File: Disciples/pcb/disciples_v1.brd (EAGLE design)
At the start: 19 x 108.4 mm, 106 parts, among them IC1 OPA1641, IC2 LM324PW, IC3 LM324PW, IC4 TL072D, IC5 LM324PW, IC6 LM4040B10, IC7 LM4040B50, J1 PJ301_THONKICONN6, J10 PJ301_THONKICONN6, J11 PJ301_THONKICONN6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

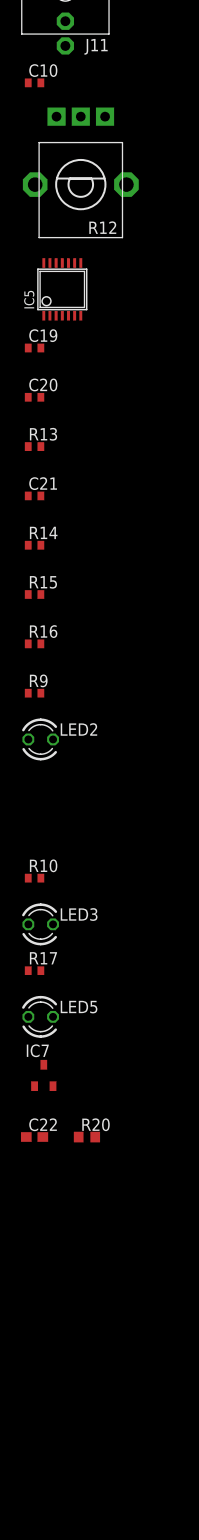
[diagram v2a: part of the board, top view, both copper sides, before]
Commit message: Comparator
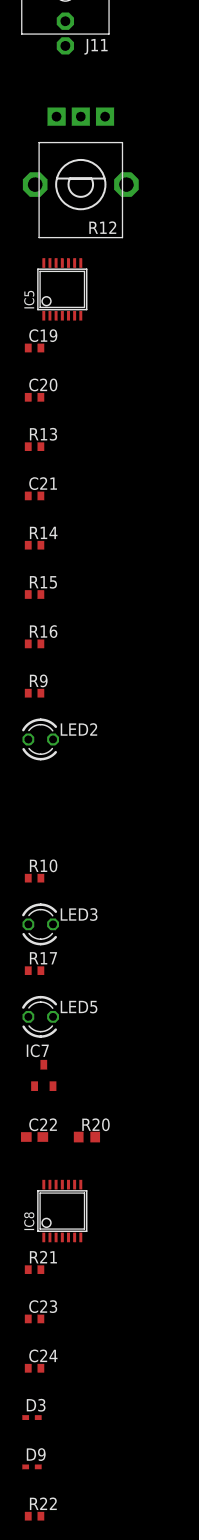
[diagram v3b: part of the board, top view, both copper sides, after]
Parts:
- removed C10: 68p, rcl:C0402
- added C23, C24: 100n, rcl:C0402
- added D3, D9: 1N4148, diode:SOD523
- added IC8: LM324PW, og-ics:TSSOP14
- added R21, R22: 1k, rcl:R0402
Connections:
- new net COMP_-12_+12: IC8.1, R21.1
- new net N$47: IC8.3, R15.2
- new net N$49: J6.P3, R22.1
- new net N$51: D3.C, IC8.7
- new net N$52: D9.A, IC8.8
- net AREF_+5: now also IC8.5
- net COMP: now also D3.A, D9.C, IC8.12, IC8.6, IC8.9, R21.2
- net GND: now also C23.2, C24.1, IC8.10
- net N$27: now also R22.2; no longer J6.P3
- net N$37: now also IC8.13
- net N$38: now also IC8.14
- net N$45: now also IC8.2
- net VCC: now also C23.1, IC8.4
- net VEE: now also C24.2, IC8.11
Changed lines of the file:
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@@
 <attribute name="NAME" x="8.31" y="-374.8875" size="1.27" layer="25" rot="R180"/>
-</element>
-<element name="C10" library="rcl" package="C0402" value="68p" x="0.635" y="-379.4125" smashed="yes">
-<attribute name="NAME" x="0" y="-378.7775" size="1.27" layer="25"/>
-<attribute name="VALUE" x="0" y="-381.3175" size="1.27" layer="27"/>
 </element>
 <element name="R12" library="og-pots" package="ALPS_POT_VERTICAL_PS" value="50k" x="5.3975" y="-389.89" smashed="yes">
@@
 <attribute name="NAME" x="0" y="-487.3625" size="1.27" layer="25"/>
 <attribute name="VALUE" x="0" y="-489.9025" size="1.27" layer="27"/>
+</element>
+<element name="IC8" library="og-ics" package="TSSOP14" value="LM324PW" x="3.4925" y="-495.6175" smashed="yes">
+<attribute name="NAME" x="0.5969" y="-497.7003" size="1.016" layer="25" ratio="10" rot="R90"/>
+<attribute name="VALUE" x="7.3787" y="-497.7003" size="1.016" layer="27" ratio="10" rot="R90"/>
+</element>
+<element name="R21" library="rcl" package="R0402" value="1k" x="0.635" y="-501.65" smashed="yes">
+<attribute name="NAME" x="0" y="-501.015" size="1.27" layer="25"/>
+<attribute name="VALUE" x="0" y="-503.555" size="1.27" layer="27"/>
+</element>
+<element name="C23" library="rcl" package="C0402" value="100n" x="0.635" y="-506.73" smashed="yes">
+<attribute name="NAME" x="0" y="-506.095" size="1.27" layer="25"/>
+<attribute name="VALUE" x="0" y="-508.635" size="1.27" layer="27"/>
+</element>
+<element name="C24" library="rcl" package="C0402" value="100n" x="0.635" y="-511.81" smashed="yes">
+<attribute name="NAME" x="0" y="-511.175" size="1.27" layer="25"/>
+<attribute name="VALUE" x="0" y="-513.715" size="1.27" layer="27"/>
+</element>
+<element name="D3" library="diode" package="SOD523" value="1N4148" x="0.3175" y="-516.89" smashed="yes">
+<attribute name="NAME" x="-0.3175" y="-516.255" size="1.27" layer="25"/>
+<attribute name="VALUE" x="-0.3175" y="-518.795" size="1.27" layer="27"/>
+</element>
+<element name="D9" library="diode" package="SOD523" value="1N4148" x="0.3175" y="-521.97" smashed="yes">
+<attribute name="NAME" x="-0.3175" y="-521.335" size="1.27" layer="25"/>
+<attribute name="VALUE" x="-0.3175" y="-523.875" size="1.27" layer="27"/>
+</element>
+<element name="R22" library="rcl" package="R0402" value="1k" x="0.635" y="-527.05" smashed="yes">
+<attribute name="NAME" x="0" y="-526.415" size="1.27" layer="25"/>
+<attribute name="VALUE" x="0" y="-528.955" size="1.27" layer="27"/>
 </element>
 </elements>
@@
 <contactref element="IC7" pad="2"/>
 <contactref element="C22" pad="2"/>
+<contactref element="C24" pad="1"/>
+<contactref element="C23" pad="2"/>
+<contactref element="IC8" pad="10"/>
+<wire x1="-0.015" y1="-511.81" x2="1.285" y2="-506.73" width="0" layer="19" extent="1-1"/>
+<wire x1="4.1275" y1="-492.8997" x2="1.285" y2="-506.73" width="0" layer="19" extent="1-1"/>
+<wire x1="1.485" y1="-487.9975" x2="4.1275" y2="-492.8997" width="0" layer="19" extent="1-1"/>
 <wire x1="2.5375" y1="-482.7475" x2="1.485" y2="-487.9975" width="0" layer="19" extent="1-1"/>
 <wire x1="1.285" y1="-470.8525" x2="2.5375" y2="-482.7475" width="0" layer="19" extent="1-1"/>
@@
 <contactref element="IC5" pad="11"/>
 <contactref element="C20" pad="2"/>
+<contactref element="IC8" pad="11"/>
+<contactref element="C24" pad="2"/>
+<wire x1="1.285" y1="-511.81" x2="3.4925" y2="-492.8997" width="0" layer="19" extent="1-1"/>
+<wire x1="1.285" y1="-411.7975" x2="3.4925" y2="-492.8997" width="0" layer="19" extent="1-1"/>
 <wire x1="3.4925" y1="-397.9672" x2="1.285" y2="-411.7975" width="0" layer="19" extent="1-1"/>
 <wire x1="1.285" y1="-302.5775" x2="3.4925" y2="-397.9672" width="0" layer="19" extent="1-1"/>
@@
 <contactref element="C19" pad="1"/>
 <contactref element="R20" pad="1"/>
+<contactref element="IC8" pad="4"/>
+<contactref element="C23" pad="1"/>
+<wire x1="3.4925" y1="-498.3353" x2="-0.015" y2="-506.73" width="0" layer="19" extent="1-1"/>
+<wire x1="5.1825" y1="-487.9975" x2="3.4925" y2="-498.3353" width="0" layer="19" extent="1-1"/>
 <wire x1="-0.015" y1="-406.7175" x2="5.1825" y2="-487.9975" width="0" layer="19" extent="1-1"/>
 <wire x1="3.4925" y1="-403.4028" x2="-0.015" y2="-406.7175" width="0" layer="19" extent="1-1"/>
@@
 <signal name="COMP">
 <contactref element="R33" pad="1"/>
+<contactref element="IC8" pad="12"/>
+<contactref element="IC8" pad="6"/>
+<contactref element="R21" pad="2"/>
+<contactref element="D3" pad="A"/>
+<contactref element="D9" pad="C"/>
+<contactref element="IC8" pad="9"/>
+<wire x1="4.7625" y1="-498.3353" x2="1.285" y2="-501.65" width="0" layer="19" extent="1-1"/>
+<wire x1="4.7625" y1="-492.8997" x2="4.7625" y2="-498.3353" width="0" layer="19" extent="1-1"/>
+<wire x1="2.8575" y1="-492.8997" x2="4.7625" y2="-492.8997" width="0" layer="19" extent="1-1"/>
+<wire x1="1.0175" y1="-516.89" x2="1.285" y2="-501.65" width="0" layer="19" extent="1-1"/>
+<wire x1="-0.2825" y1="-521.97" x2="1.0175" y2="-516.89" width="0" layer="19" extent="1-1"/>
+<wire x1="9.8275" y1="-108.2675" x2="4.7625" y2="-492.8997" width="0" layer="19" extent="1-1"/>
 </signal>
 <signal name="N$28">
@@
 <wire x1="2.2225" y1="-403.4028" x2="1.285" y2="-461.3275" width="0" layer="19" extent="1-1"/>
 </signal>
-<signal name="N$27">
-<contactref element="C17" pad="1"/>
-<contactref element="J6" pad="P3"/>
-<wire x1="-0.215" y1="-292.4175" x2="3.81" y2="-50.165" width="0" layer="19" extent="1-1"/>
-</signal>
 <signal name="N$32">
 <contactref element="C17" pad="2"/>
@@
 <signal name="N$45">
 <contactref element="R16" pad="2"/>
+<contactref element="IC8" pad="2"/>
+<wire x1="1.285" y1="-437.1975" x2="2.2225" y2="-498.3353" width="0" layer="19" extent="1-1"/>
 </signal>
 <signal name="N$46">
@@
 <contactref element="R17" pad="1"/>
 <contactref element="LED5" pad="K"/>
+<contactref element="IC8" pad="13"/>
+<wire x1="2.54" y1="-475.615" x2="2.2225" y2="-492.8997" width="0" layer="19" extent="1-1"/>
 <wire x1="-0.015" y1="-470.8525" x2="2.54" y2="-475.615" width="0" layer="19" extent="1-1"/>
 </signal>
 <signal name="N$38">
 <contactref element="LED5" pad="A"/>
+<contactref element="IC8" pad="14"/>
+<wire x1="0" y1="-475.615" x2="1.5875" y2="-492.8997" width="0" layer="19" extent="1-1"/>
 </signal>
 <signal name="AREF_+5">
@@
 <contactref element="R20" pad="2"/>
 <contactref element="C22" pad="1"/>
+<contactref element="IC8" pad="5"/>
+<wire x1="6.8825" y1="-487.9975" x2="4.1275" y2="-498.3353" width="0" layer="19" extent="1-1"/>
+<wire x1="-0.215" y1="-487.9975" x2="6.8825" y2="-487.9975" width="0" layer="19" extent="1-1"/>
 <wire x1="0.6375" y1="-482.7475" x2="-0.215" y2="-487.9975" width="0" layer="19" extent="1-1"/>
-<wire x1="6.8825" y1="-487.9975" x2="-0.215" y2="-487.9975" width="0" layer="19" extent="1-1"/>
+</signal>
+<signal name="N$47">
+<contactref element="R15" pad="2"/>
+<contactref element="IC8" pad="3"/>
+<wire x1="1.285" y1="-432.1175" x2="2.8575" y2="-498.3353" width="0" layer="19" extent="1-1"/>
+</signal>
+<signal name="COMP_-12_+12">
+<contactref element="IC8" pad="1"/>
+<contactref element="R21" pad="1"/>
+<wire x1="1.5875" y1="-498.3353" x2="-0.015" y2="-501.65" width="0" layer="19" extent="1-1"/>
+</signal>
+<signal name="N$51">
+<contactref element="IC8" pad="7"/>
+<contactref element="D3" pad="C"/>
+<wire x1="-0.2825" y1="-516.89" x2="5.3975" y2="-498.3353" width="0" layer="19" extent="1-1"/>
+</signal>
+<signal name="N$52">
+<contactref element="IC8" pad="8"/>
+<contactref element="D9" pad="A"/>
+<wire x1="1.0175" y1="-521.97" x2="5.3975" y2="-492.8997" width="0" layer="19" extent="1-1"/>
+</signal>
+<signal name="N$27">
+<contactref element="R22" pad="2"/>
+<contactref element="C17" pad="1"/>
+<wire x1="1.285" y1="-527.05" x2="-0.215" y2="-292.4175" width="0" layer="19" extent="1-1"/>
+</signal>
+<signal name="N$49">
+<contactref element="J6" pad="P3"/>
+<contactref element="R22" pad="1"/>
+<wire x1="-0.015" y1="-527.05" x2="3.81" y2="-50.165" width="0" layer="19" extent="1-1"/>
 </signal>
 </signals>

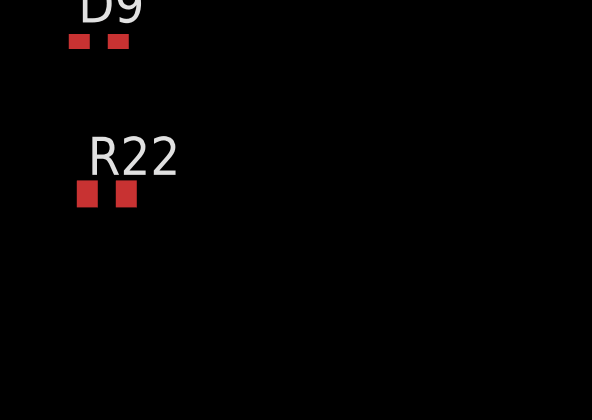
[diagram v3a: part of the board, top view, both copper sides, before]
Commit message: Added slow slew cap (no sw yet)
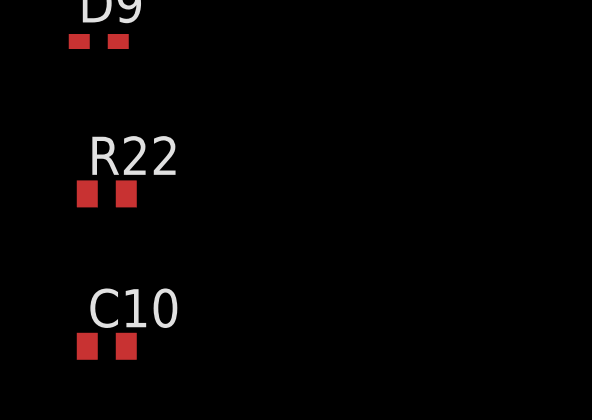
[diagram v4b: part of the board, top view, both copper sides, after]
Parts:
- added C10: 100u, rcl:C0402
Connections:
- net SLEW: now also C10.2
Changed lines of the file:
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@@
 <attribute name="VALUE" x="0" y="-528.955" size="1.27" layer="27"/>
+</element>
+<element name="C10" library="rcl" package="C0402" value="100u" x="0.635" y="-532.13" smashed="yes">
+<attribute name="NAME" x="0" y="-531.495" size="1.27" layer="25"/>
+<attribute name="VALUE" x="0" y="-534.035" size="1.27" layer="27"/>
 </element>
 </elements>
@@
 </signal>
 <signal name="SLEW">
-<contactref element="C11" pad="2"/>
 <contactref element="R28" pad="2"/>
 <contactref element="R2" pad="1"/>
@@
 <contactref element="J8" pad="P2"/>
 <contactref element="IC5" pad="3"/>
-<wire x1="1.6025" y1="-223.2025" x2="6.365" y2="-228.2825" width="0" layer="19" extent="1-1"/>
+<contactref element="C11" pad="2"/>
+<contactref element="C10" pad="2"/>
+<wire x1="6.365" y1="-228.2825" x2="1.6025" y2="-223.2025" width="0" layer="19" extent="1-1"/>
 <wire x1="3.81" y1="-341.9475" x2="6.365" y2="-228.2825" width="0" layer="19" extent="1-1"/>
 <wire x1="2.8575" y1="-403.4028" x2="3.81" y2="-341.9475" width="0" layer="19" extent="1-1"/>
+<wire x1="1.285" y1="-532.13" x2="2.8575" y2="-403.4028" width="0" layer="19" extent="1-1"/>
 <wire x1="0.3025" y1="-90.17" x2="1.6025" y2="-223.2025" width="0" layer="19" extent="1-1"/>
 <wire x1="12.2428" y1="10.16" x2="0.3025" y2="-90.17" width="0" layer="19" extent="1-1"/>
@@
 <contactref element="R18" pad="P$2"/>
 <contactref element="R19" pad="P$2"/>
+<contactref element="IC3" pad="9"/>
 <contactref element="C11" pad="1"/>
-<contactref element="IC3" pad="9"/>
 <wire x1="5.3975" y1="-306.055" x2="5.065" y2="-228.2825" width="0" layer="19" extent="1-1"/>
 <wire x1="5.3975" y1="-320.025" x2="5.3975" y2="-306.055" width="0" layer="19" extent="1-1"/>

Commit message: CV Pot
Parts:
- added C25, C26: 100n, rcl:C0402
- added IC9: LM324PW, og-ics:TSSOP14
- added J12: PJ301_THONKICONN6, og-pj301:WQP_PJ_301M6
- added R24: 50k, og-pots:ALPS_POT_VERTICAL_PS
- added R27: 510, rcl:R0402
- C21: value TBD -> (none)
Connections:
- new net N$50: IC9.3, R24.P$2
- new net N$53: J12.P3, R27.2
- net AREF_+5: now also R24.P$3
- net GND: now also C25.2, C26.1, J12.P1
- net THRESH: now also IC9.1, IC9.2, R27.1
- net VCC: now also C25.1, IC9.4
- net VEE: now also C26.2, IC9.11
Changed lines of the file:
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@@
 <attribute name="VALUE" x="0" y="-418.7825" size="1.27" layer="27"/>
 </element>
-<element name="C21" library="rcl" package="C0402" value="TBD" x="0.635" y="-421.9575" smashed="yes">
+<element name="C21" library="rcl" package="C0402" value="" x="0.635" y="-421.9575" smashed="yes">
 <attribute name="NAME" x="0" y="-421.3225" size="1.27" layer="25"/>
 <attribute name="VALUE" x="0" y="-423.8625" size="1.27" layer="27"/>
@@
 <attribute name="NAME" x="0" y="-531.495" size="1.27" layer="25"/>
 <attribute name="VALUE" x="0" y="-534.035" size="1.27" layer="27"/>
+</element>
+<element name="IC9" library="og-ics" package="TSSOP14" value="LM324PW" x="3.4925" y="-539.75" smashed="yes">
+<attribute name="NAME" x="0.5969" y="-541.8328" size="1.016" layer="25" ratio="10" rot="R90"/>
+<attribute name="VALUE" x="7.3787" y="-541.8328" size="1.016" layer="27" ratio="10" rot="R90"/>
+</element>
+<element name="R24" library="og-pots" package="ALPS_POT_VERTICAL_PS" value="50k" x="5.3975" y="-551.18" smashed="yes">
+<attribute name="NAME" x="9.2075" y="-554.99" size="1.27" layer="25" rot="R180"/>
+<attribute name="VALUE" x="9.2075" y="-553.466" size="1.27" layer="27" rot="R180"/>
+</element>
+<element name="J12" library="og-pj301" package="WQP_PJ_301M6" value="PJ301_THONKICONN6" x="3.81" y="-562.9275" smashed="yes">
+<attribute name="NAME" x="8.31" y="-567.9275" size="1.27" layer="25" rot="R180"/>
+</element>
+<element name="R27" library="rcl" package="R0402" value="510" x="0.635" y="-572.4525" smashed="yes">
+<attribute name="NAME" x="0" y="-571.8175" size="1.27" layer="25"/>
+<attribute name="VALUE" x="0" y="-574.3575" size="1.27" layer="27"/>
+</element>
+<element name="C25" library="rcl" package="C0402" value="100n" x="0.635" y="-577.5325" smashed="yes">
+<attribute name="NAME" x="0" y="-576.8975" size="1.27" layer="25"/>
+<attribute name="VALUE" x="0" y="-579.4375" size="1.27" layer="27"/>
+</element>
+<element name="C26" library="rcl" package="C0402" value="100n" x="0.635" y="-582.6125" smashed="yes">
+<attribute name="NAME" x="0" y="-581.9775" size="1.27" layer="25"/>
+<attribute name="VALUE" x="0" y="-584.5175" size="1.27" layer="27"/>
 </element>
 </elements>
@@
 <contactref element="C23" pad="2"/>
 <contactref element="IC8" pad="10"/>
+<contactref element="J12" pad="P1"/>
+<contactref element="C26" pad="1"/>
+<contactref element="C25" pad="2"/>
 <wire x1="-0.015" y1="-511.81" x2="1.285" y2="-506.73" width="0" layer="19" extent="1-1"/>
 <wire x1="4.1275" y1="-492.8997" x2="1.285" y2="-506.73" width="0" layer="19" extent="1-1"/>
@@
 <wire x1="0.505" y1="-286.7025" x2="1.285" y2="-297.4975" width="0" layer="19" extent="1-1"/>
 <wire x1="3.305" y1="-280.3525" x2="0.505" y2="-286.7025" width="0" layer="19" extent="1-1"/>
+<wire x1="3.81" y1="-568.6425" x2="-0.015" y2="-511.81" width="0" layer="19" extent="1-1"/>
+<wire x1="1.285" y1="-577.5325" x2="3.81" y2="-568.6425" width="0" layer="19" extent="1-1"/>
+<wire x1="-0.015" y1="-582.6125" x2="1.285" y2="-577.5325" width="0" layer="19" extent="1-1"/>
 <wire x1="1.8025" y1="-199.39" x2="3.305" y2="-280.3525" width="0" layer="19" extent="1-1"/>
 <wire x1="2.855" y1="-194.14" x2="1.8025" y2="-199.39" width="0" layer="19" extent="1-1"/>
@@
 <contactref element="IC8" pad="11"/>
 <contactref element="C24" pad="2"/>
+<contactref element="IC9" pad="11"/>
+<contactref element="C26" pad="2"/>
 <wire x1="1.285" y1="-511.81" x2="3.4925" y2="-492.8997" width="0" layer="19" extent="1-1"/>
+<wire x1="3.4925" y1="-537.0322" x2="1.285" y2="-511.81" width="0" layer="19" extent="1-1"/>
+<wire x1="1.285" y1="-582.6125" x2="3.4925" y2="-537.0322" width="0" layer="19" extent="1-1"/>
 <wire x1="1.285" y1="-411.7975" x2="3.4925" y2="-492.8997" width="0" layer="19" extent="1-1"/>
 <wire x1="3.4925" y1="-397.9672" x2="1.285" y2="-411.7975" width="0" layer="19" extent="1-1"/>
@@
 <contactref element="IC8" pad="4"/>
 <contactref element="C23" pad="1"/>
+<contactref element="IC9" pad="4"/>
+<contactref element="C25" pad="1"/>
 <wire x1="3.4925" y1="-498.3353" x2="-0.015" y2="-506.73" width="0" layer="19" extent="1-1"/>
 <wire x1="5.1825" y1="-487.9975" x2="3.4925" y2="-498.3353" width="0" layer="19" extent="1-1"/>
+<wire x1="3.4925" y1="-542.4678" x2="-0.015" y2="-506.73" width="0" layer="19" extent="1-1"/>
+<wire x1="-0.015" y1="-577.5325" x2="3.4925" y2="-542.4678" width="0" layer="19" extent="1-1"/>
 <wire x1="-0.015" y1="-406.7175" x2="5.1825" y2="-487.9975" width="0" layer="19" extent="1-1"/>
 <wire x1="3.4925" y1="-403.4028" x2="-0.015" y2="-406.7175" width="0" layer="19" extent="1-1"/>
@@
 <signal name="FULL_WAVE_RECT">
 <contactref element="R34" pad="2"/>
+<contactref element="J7" pad="P2"/>
+<contactref element="IC2" pad="12"/>
 <contactref element="R36" pad="1"/>
-<contactref element="J7" pad="P2"/>
 <contactref element="IC2" pad="8"/>
-<contactref element="IC2" pad="12"/>
 <wire x1="6.0175" y1="-41.91" x2="3.81" y2="-70.8025" width="0" layer="19" extent="1-1"/>
 <wire x1="12.715" y1="-16.51" x2="6.0175" y2="-41.91" width="0" layer="19" extent="1-1"/>
@@
 <signal name="THRESH">
 <contactref element="J10" pad="P2"/>
+<contactref element="IC9" pad="2"/>
+<contactref element="IC9" pad="1"/>
+<contactref element="R27" pad="1"/>
+<wire x1="2.2225" y1="-542.4678" x2="3.81" y2="-127.9525" width="0" layer="19" extent="1-1"/>
+<wire x1="1.5875" y1="-542.4678" x2="2.2225" y2="-542.4678" width="0" layer="19" extent="1-1"/>
+<wire x1="-0.015" y1="-572.4525" x2="1.5875" y2="-542.4678" width="0" layer="19" extent="1-1"/>
 </signal>
 <signal name="N$34">
@@
 </signal>
 <signal name="LOWPASS">
-<contactref element="R23" pad="1"/>
 <contactref element="J11" pad="P2"/>
 <contactref element="IC5" pad="9"/>
+<contactref element="IC5" pad="12"/>
 <contactref element="IC5" pad="8"/>
-<contactref element="IC5" pad="12"/>
+<contactref element="R23" pad="1"/>
 <wire x1="5.3975" y1="-397.9672" x2="4.7625" y2="-397.9672" width="0" layer="19" extent="1-1"/>
 <wire x1="2.8575" y1="-397.9672" x2="4.7625" y2="-397.9672" width="0" layer="19" extent="1-1"/>
@@
 <contactref element="C22" pad="1"/>
 <contactref element="IC8" pad="5"/>
+<contactref element="R24" pad="P$3"/>
 <wire x1="6.8825" y1="-487.9975" x2="4.1275" y2="-498.3353" width="0" layer="19" extent="1-1"/>
 <wire x1="-0.215" y1="-487.9975" x2="6.8825" y2="-487.9975" width="0" layer="19" extent="1-1"/>
 <wire x1="0.6375" y1="-482.7475" x2="-0.215" y2="-487.9975" width="0" layer="19" extent="1-1"/>
+<wire x1="7.8975" y1="-544.18" x2="4.1275" y2="-498.3353" width="0" layer="19" extent="1-1"/>
 </signal>
 <signal name="N$47">
@@
 <wire x1="-0.015" y1="-527.05" x2="3.81" y2="-50.165" width="0" layer="19" extent="1-1"/>
 </signal>
+<signal name="N$50">
+<contactref element="IC9" pad="3"/>
+<contactref element="R24" pad="P$2"/>
+<wire x1="5.3975" y1="-544.18" x2="2.8575" y2="-542.4678" width="0" layer="19" extent="1-1"/>
+</signal>
+<signal name="N$53">
+<contactref element="J12" pad="P3"/>
+<contactref element="R27" pad="2"/>
+<wire x1="3.81" y1="-558.4825" x2="1.285" y2="-572.4525" width="0" layer="19" extent="1-1"/>
+</signal>
 </signals>
